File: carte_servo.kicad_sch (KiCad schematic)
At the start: 61 parts, among them J15 Conn_01x04_Pin, J16 Conn_01x05, J17 Conn_01x05, J2 Conn_02x04_Top_Bottom, J22 Conn_02x04_Top_Bottom, J23 Conn_01x05, J24 Conn_LEDs, SW1 SW_Reset, SW2 SW_Boot, U1 XGZP6897D_differential_pressu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

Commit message: fix error + add fuse/resistor choice servo DCDC vin = 12V or 24V
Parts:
- added C40, C41: 10uF, Capacitor_SMD:C_0805_2012Metric, symbol Device:C
- added D9: 13V, Diode_SMD:D_SOD-123, symbol Device:D_Zener
- added F3: Fuse 4A, Fuse:Fuse_Littelfuse-NANO2-451_453, symbol Device:Fuse
- added R66: R_Select_12V_servo_in, Resistor_SMD:R_1206_3216Metric, symbol Device:R_Small
- added R68: R_Select_24V_servo_in, Resistor_SMD:R_1206_3216Metric, symbol Device:R_Small
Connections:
- net 24V_POW_P: now also F3.2
- net BATT_12V: now also R66.1
- net GND: now also C40.2, C41.2, D9.2 (A)
- net ENABLE renamed EnableESP32
- new net BATT_24V_power: C40.1, C41.1, D9.1 (K), F3.1, R68.1
- new net ServoDCDC/VIN: R66.2, R68.2
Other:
- sheet stepper_driver ports: added EnableStepper; removed Enable
- sheet stepper_driver1 ports: added EnableStepper; removed Enable

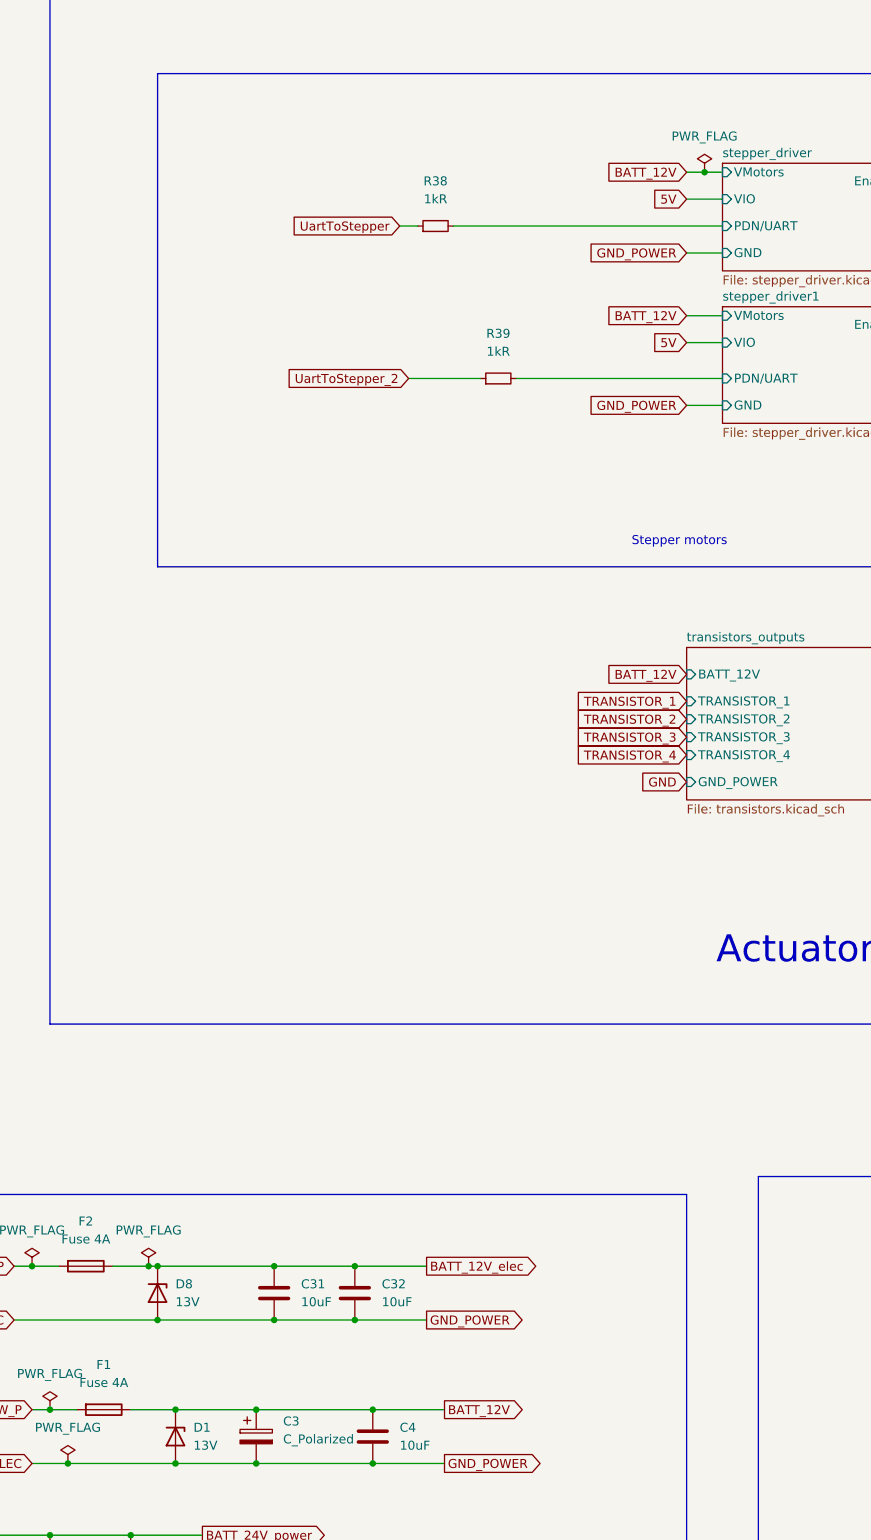
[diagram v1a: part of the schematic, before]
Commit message: fix AX12 RX: add proper 3.3V/5V level shifter
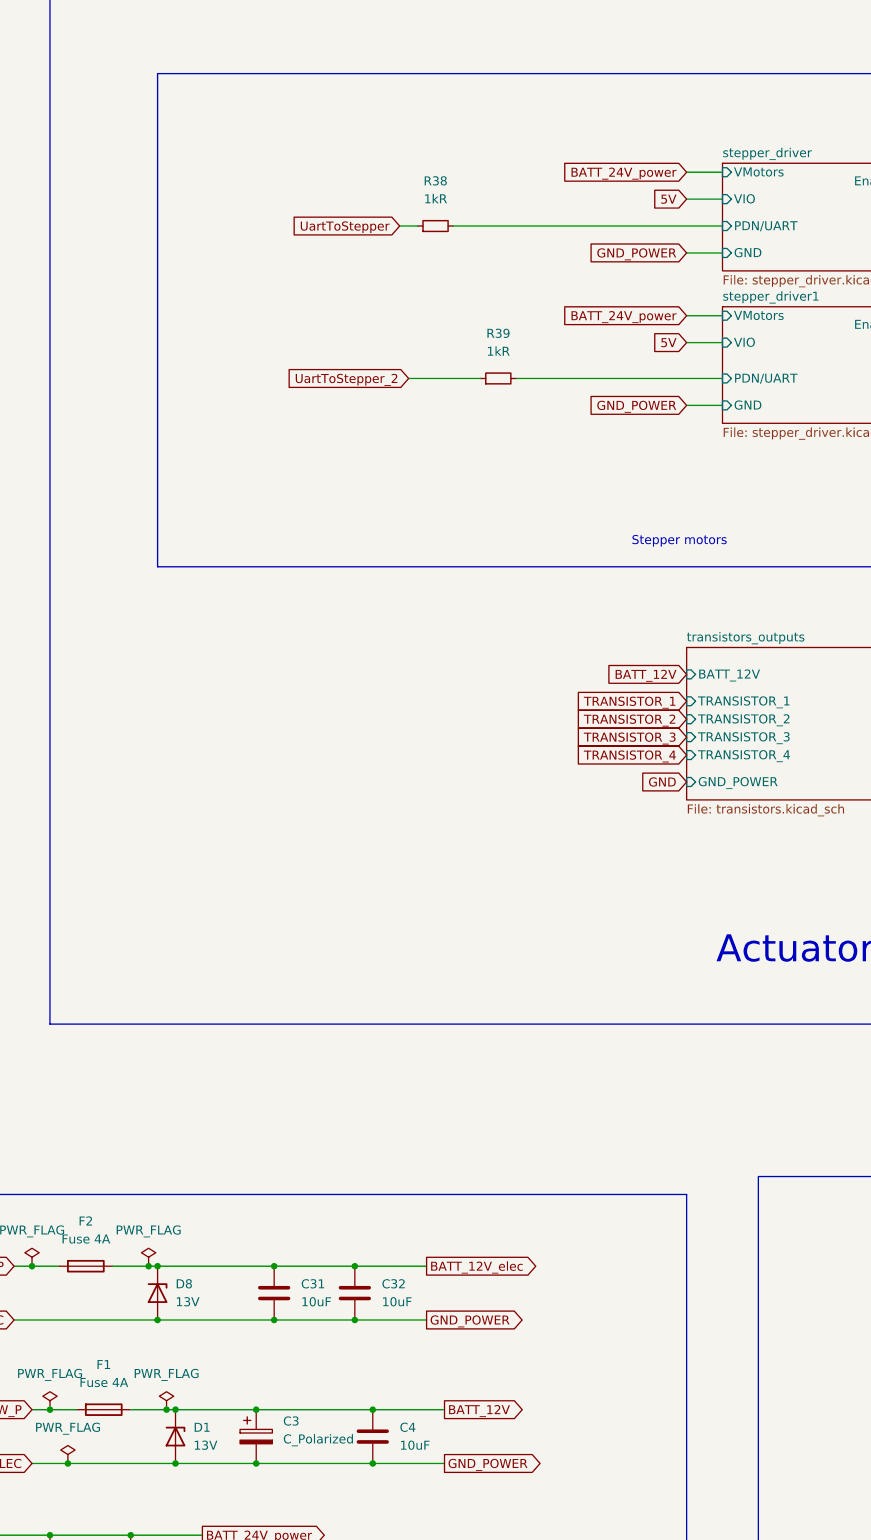
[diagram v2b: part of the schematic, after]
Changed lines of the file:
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@@
 	)
 	(junction
-		(at 476.25 153.67)
-		(diameter 0)
-		(color 0 0 0 0)
-	)
-	(junction
 		(at 163.83 100.33)
 		(diameter 0)
@@
 	)
 	(junction
+		(at 400.05 328.93)
+		(diameter 0)
+		(color 0 0 0 0)
+	)
+	(junction
 		(at 111.76 358.14)
 		(diameter 0)
@@
 	(wire
 		(pts
-			(xy 394.97 328.93) (xy 401.32 328.93)
+			(xy 394.97 328.93) (xy 400.05 328.93)
 		)
 		(stroke
@@
 	(wire
 		(pts
+			(xy 400.05 328.93) (xy 401.32 328.93)
+		)
+		(stroke
+			(width 0)
+			(type default)
+		)
+	)
+	(wire
+		(pts
 			(xy 401.32 328.93) (xy 412.75 328.93)
 		)
@@
 	(wire
 		(pts
-			(xy 476.25 153.67) (xy 478.79 153.67)
+			(xy 473.71 153.67) (xy 478.79 153.67)
 		)
 		(stroke
@@
 	(wire
 		(pts
-			(xy 473.71 153.67) (xy 476.25 153.67)
-		)
-		(stroke
-			(width 0)
-			(type default)
-		)
-	)
-	(wire
-		(pts
 			(xy 302.26 327.66) (xy 304.8 327.66)
 		)
@@
 		)
 	)
-	(global_label "BATT_12V"
-		(shape input)
-		(at 473.71 153.67 180)
-		(fields_autoplaced yes)
-		(effects
-			(font
-				(size 1.27 1.27)
-			)
-			(justify right)
-		)
-		(property "Intersheetrefs" "${INTERSHEET_REFS}"
-			(at 462.5279 153.5906 0)
-			(effects
-				(font
-					(size 1.27 1.27)
-				)
-				(justify right)
-				(hide yes)
-			)
-		)
-	)
 	(global_label "24V_POW_P"
 		(shape input)
@@
 		)
 	)
-	(global_label "BATT_12V"
-		(shape input)
-		(at 473.71 173.99 180)
-		(fields_autoplaced yes)
-		(effects
-			(font
-				(size 1.27 1.27)
-			)
-			(justify right)
-		)
-		(property "Intersheetrefs" "${INTERSHEET_REFS}"
-			(at 462.5279 173.9106 0)
-			(effects
-				(font
-					(size 1.27 1.27)
-				)
-				(justify right)
-				(hide yes)
-			)
-		)
-	)
 	(global_label "GND"
 		(shape input)
@@
 	(global_label "BATT_24V_power"
 		(shape input)
+		(at 473.71 173.99 180)
+		(fields_autoplaced yes)
+		(effects
+			(font
+				(size 1.27 1.27)
+			)
+			(justify right)
+		)
+		(property "Intersheetrefs" "${INTERSHEET_REFS}"
+			(at 455.4849 173.99 0)
+			(effects
+				(font
+					(size 1.27 1.27)
+				)
+				(justify right)
+				(hide yes)
+			)
+		)
+	)
+	(global_label "BATT_24V_power"
+		(shape input)
 		(at 421.64 62.23 180)
 		(fields_autoplaced yes)
@@
 		)
 	)
+	(global_label "BATT_24V_power"
+		(shape input)
+		(at 473.71 153.67 180)
+		(fields_autoplaced yes)
+		(effects
+			(font
+				(size 1.27 1.27)
+			)
+			(justify right)
+		)
+		(property "Intersheetrefs" "${INTERSHEET_REFS}"
+			(at 455.4849 153.67 0)
+			(effects
+				(font
+					(size 1.27 1.27)
+				)
+				(justify right)
+				(hide yes)
+			)
+		)
+	)
 	(global_label "GND_ELEC"
 		(shape input)
@@
 	)
 	(symbol
+		(lib_id "power:PWR_FLAG")
+		(at 400.05 328.93 0)
+		(unit 1)
+		(exclude_from_sim no)
+		(in_bom yes)
+		(on_board yes)
+		(dnp no)
+		(fields_autoplaced yes)
+		(property "Reference" "#FLG10"
+			(at 400.05 327.025 0)
+			(effects
+				(font
+					(size 1.27 1.27)
+				)
+				(hide yes)
+			)
+		)
+		(property "Value" "PWR_FLAG"
+			(at 400.05 323.85 0)
+			(effects
+				(font
+					(size 1.27 1.27)
+				)
+			)
+		)
+		(property "Footprint" ""
+			(at 400.05 328.93 0)
+			(effects
+				(font
+					(size 1.27 1.27)
+				)
+				(hide yes)
+			)
+		)
+		(property "Datasheet" "~"
+			(at 400.05 328.93 0)
+			(effects
+				(font
+					(size 1.27 1.27)
+				)
+				(hide yes)
+			)
+		)
+		(property "Description" "Special symbol for telling ERC where power comes from"
+			(at 400.05 328.93 0)
+			(effects
+				(font
+					(size 1.27 1.27)
+				)
+				(hide yes)
+			)
+		)
+		(pin "1"
+		)
+		(instances
+			(project "carte_servo"
+				(path "/e63e39d7-6ac0-4ffd-8aa3-1841a4541b55"
+					(reference "#FLG10")
+					(unit 1)
+				)
+			)
+		)
+	)
+	(symbol
 		(lib_id "Device:C")
 		(at 213.36 196.85 0)
@@
 					(unit 1)
 				)
-			)
-		)
-	)
-	(symbol
-		(lib_id "power:PWR_FLAG")
-		(at 476.25 153.67 0)
-		(unit 1)
-		(exclude_from_sim no)
-		(in_bom yes)
-		(on_board yes)
-		(dnp no)
-		(fields_autoplaced yes)
-		(property "Reference" "#FLG04"
-			(at 476.25 151.765 0)
-			(effects
-				(font
-					(size 1.27 1.27)
-				)
-				(hide yes)
-			)
-		)
-		(property "Value" "PWR_FLAG"
-			(at 476.25 148.59 0)
-			(effects
-				(font
-					(size 1.27 1.27)
-				)
-			)
-		)
-		(property "Footprint" ""
-			(at 476.25 153.67 0)
-			(effects
-				(font
-					(size 1.27 1.27)
-				)
-				(hide yes)
-			)
-		)
-		(property "Datasheet" "~"
-			(at 476.25 153.67 0)
-			(effects
-				(font
-					(size 1.27 1.27)
-				)
-				(hide yes)
-			)
-		)
-		(property "Description" "Special symbol for telling ERC where power comes from"
-			(at 476.25 153.67 0)
-			(effects
-				(font
-					(size 1.27 1.27)
-				)
-				(hide yes)
-			)
-		)
-		(pin "1"
-		)
-		(instances
-			(project "carte_servo"
-				(path "/e63e39d7-6ac0-4ffd-8aa3-1841a4541b55"
-					(reference "#FLG04")
-					(unit 1)
-				)

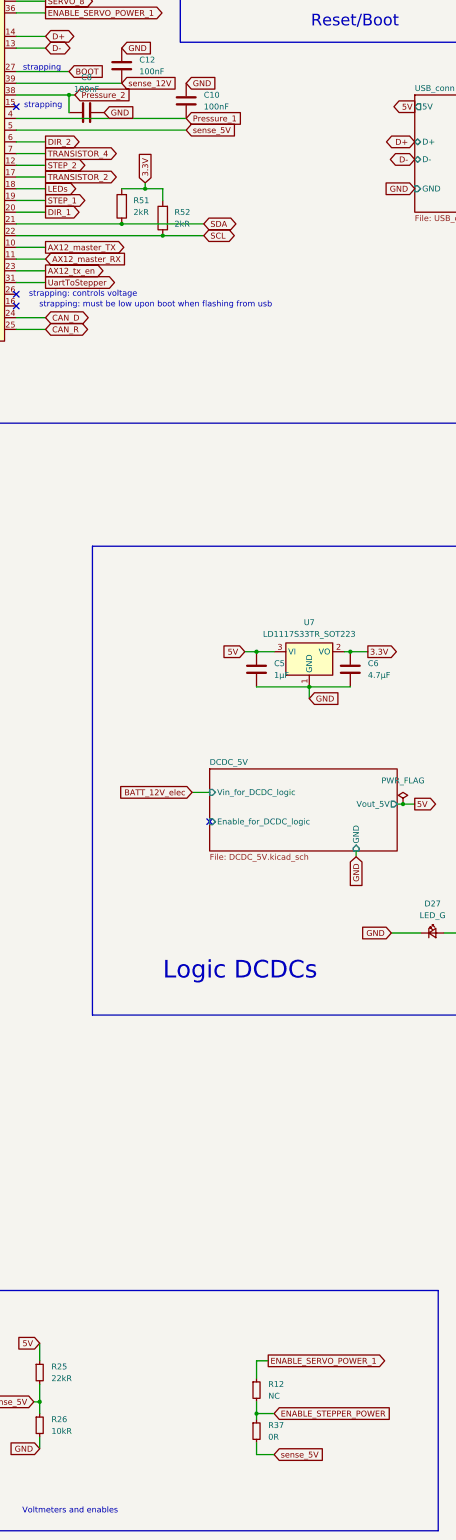
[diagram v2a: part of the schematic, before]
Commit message: add 12V elec measure
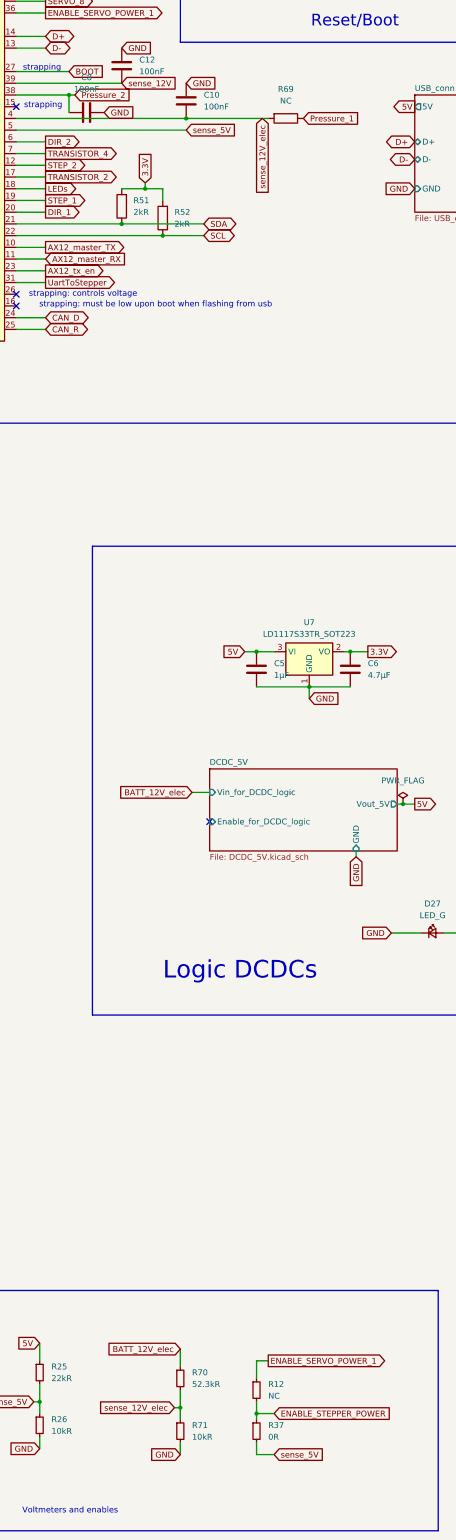
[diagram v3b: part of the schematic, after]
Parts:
- added R69: NC, Resistor_SMD:R_0603_1608Metric, symbol Device:R
- added R70: 52.3kR, Resistor_SMD:R_0603_1608Metric, symbol Device:R_Small
- added R71: 10kR, Resistor_SMD:R_0603_1608Metric, symbol Device:R_Small
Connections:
- net BATT_12V_elec: now also R70.1
- net GND: now also R71.2
- net Pressure_1: now also R69.1; no longer C10.2, U8.4 (GPIO4/TOUCH4/ADC1_CH3)
- new net sense_12V_elec: C10.2, R69.2, R70.2, R71.1, U8.4 (GPIO4/TOUCH4/ADC1_CH3)

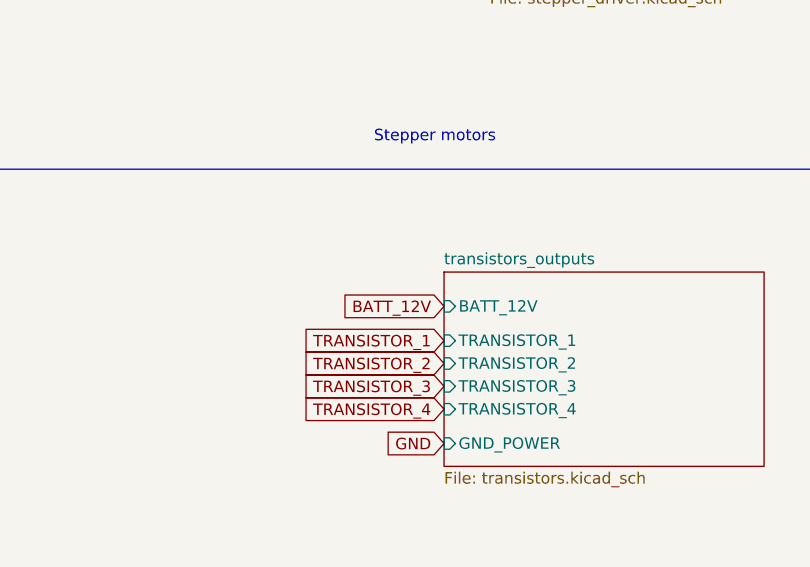
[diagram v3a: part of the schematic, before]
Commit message: add possibility to have 2 of the transistor outputs to use either 12V or 24V
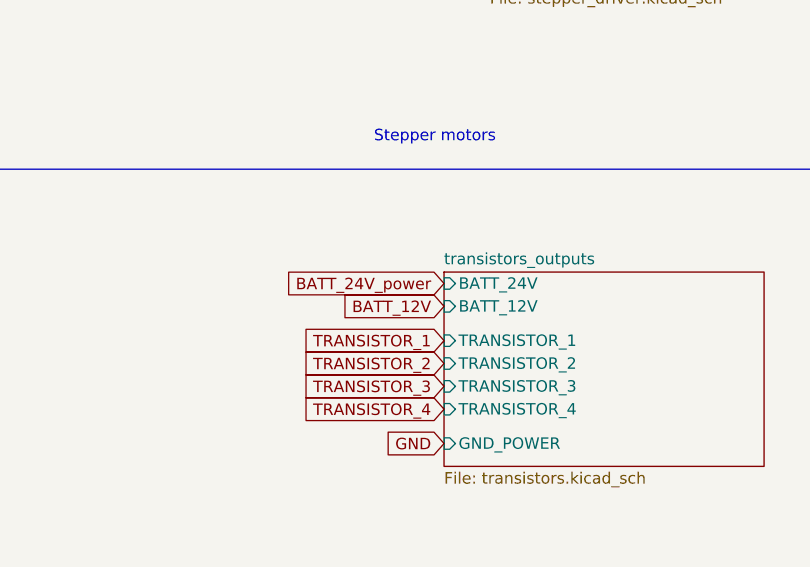
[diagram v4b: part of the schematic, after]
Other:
- sheet transistors_outputs ports: added BATT_24V; removed none
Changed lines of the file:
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@@
 		)
 	)
+	(global_label "BATT_24V_power"
+		(shape input)
+		(at 473.71 222.25 180)
+		(fields_autoplaced yes)
+		(effects
+			(font
+				(size 1.27 1.27)
+			)
+			(justify right)
+		)
+		(property "Intersheetrefs" "${INTERSHEET_REFS}"
+			(at 455.4849 222.25 0)
+			(effects
+				(font
+					(size 1.27 1.27)
+				)
+				(justify right)
+				(hide yes)
+			)
+		)
+	)
 	(global_label "BATT_12V"
 		(shape input)
@@
 			(effects
 				(font
+					(size 1.27 1.27)
+				)
+				(justify left)
+			)
+		)
+		(pin "BATT_24V" input
+			(at 473.71 222.25 180)
+			(effects
+				(font
